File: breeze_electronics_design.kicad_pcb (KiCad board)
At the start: 2 copper layers, 0 parts

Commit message: Delete the footprint of components
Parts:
- added ANT1: Antenna, Footprint:SMD_AN9520, F.Cu at (178.3, 103.0)
- added C1: 0.1UF, Capacitors_SMD:C_0402, F.Cu at (215.7, 133.5)
- added C10: 10UF, Capacitors_SMD:C_1206, F.Cu at (183.8, 111.7)
- added C11: 0.1UF, Capacitors_SMD:C_0402, F.Cu at (234.8, 127.1)
- added C12: 2.2UF, Capacitors_SMD:C_0402, F.Cu at (253.6, 98.1)
- added C13: 220PF, Capacitors_SMD:C_0402, F.Cu at (249.0, 109.3)
- added C14: 2.2UF, Capacitors_SMD:C_0402, F.Cu at (241.8, 115.0)
- added C15: 0.1UF, Capacitors_SMD:C_0402, F.Cu at (217.7, 139.0)
- added C16: 2.2UF, Capacitors_SMD:C_0402, F.Cu at (230.0, 127.1)
- added C17: 220NF, Capacitors_SMD:C_0402, F.Cu at (235.0, 121.6)
- added C18: 0.1UF, Capacitors_SMD:C_0402, F.Cu at (251.4, 103.6)
- added C19: 4.7UF, Capacitors_SMD:C_0402, F.Cu at (230.0, 121.6)
- added C2: 2.2UF, Capacitors_SMD:C_0402, F.Cu at (232.2, 132.6)
- added C20: 2.2UF, Capacitors_SMD:C_0402, F.Cu at (212.9, 139.2)
- added C21: 2.2UF, Capacitors_SMD:C_0402, F.Cu at (237.0, 116.1)
- added C22: 2.2NF, Capacitors_SMD:C_0402, F.Cu at (243.9, 109.5)
- added C23: 2.2UF, Capacitors_SMD:C_0402, F.Cu at (208.1, 145.6)
- added C24: 0.1UF, Capacitors_SMD:C_0402, F.Cu at (221.7, 131.1)
- added C25: 2.2UF, Capacitors_SMD:C_0402, F.Cu at (212.9, 144.7)
- added C26: 22PF, Capacitors_SMD:C_0402, F.Cu at (239.4, 109.5)
- added C27: 2.2NF, Capacitors_SMD:C_0402, F.Cu at (246.5, 103.8)
- added C28: 4.7PF, Capacitors_SMD:C_0402, F.Cu at (202.3, 145.8)
- added C29: 22PF, Capacitors_SMD:C_0402, F.Cu at (232.4, 116.1)
- added C3: 2.2UF, Capacitors_SMD:C_0402, F.Cu at (225.1, 125.6)
- added C30: 1.5PF, Capacitors_SMD:C_0402, F.Cu at (208.1, 140.1)
- added C31: 1PF, Capacitors_SMD:C_0402, F.Cu at (221.0, 125.6)
- added C32: 0.1UF, Capacitors_SMD:C_0402, F.Cu at (248.8, 98.1)
- added C33: 2.2UF, Capacitors_SMD:C_0402, F.Cu at (192.1, 146.6)
- added C4: 2.2UF, Capacitors_SMD:C_0402, F.Cu at (217.7, 144.5)
- added C5: 2.2UF, Capacitors_SMD:C_0402, F.Cu at (227.4, 132.6)
- added C6: 0.1UF, Capacitors_SMD:C_0402, F.Cu at (240.1, 121.6)
- added C7: 2.2UF, Capacitors_SMD:C_0402, F.Cu at (222.5, 136.6)
- added C8: 0.1UF, Capacitors_SMD:C_0402, F.Cu at (246.6, 115.0)
- added C9: 10UF, Capacitors_SMD:C_1206, F.Cu at (215.0, 114.0)
- added D1: MBR0520, Diodes_SMD:SOD-123, F.Cu at (200.3, 124.6)
- added D2: MBR0520, Diodes_SMD:SOD-123, F.Cu at (216.2, 107.5)
- added H1: Header, Pin_Headers:Pin_Header_Straight_1x02, F.Cu at (200.9, 101.5)
- added J1: SIP4, Pin_Headers:Pin_Header_Straight_1x04, F.Cu at (162.0, 125.4)
- added L1: 4.7UH, Footprint:SMD_L0402, F.Cu at (222.4, 141.9)
- added L2: 8.2NH, Footprint:SMD_L0402, F.Cu at (244.8, 120.3)
- added L3: 2.7NH, Footprint:SMD_L0402, F.Cu at (239.5, 126.9)
- added L4: 3.9NH, Footprint:SMD_L0402, F.Cu at (251.3, 114.6)
- added LED1: POWER, LEDs:LED_0603, F.Cu at (166.8, 132.6)
- added LED10: BT_LED, LEDs:LED_0603, F.Cu at (199.3, 137.3)
- added LED11: CHG_LED, LEDs:LED_0603, F.Cu at (186.1, 142.7)
- added LED2: M1_LED_TOP, LEDs:LED_0603, F.Cu at (184.2, 124.1)
- added LED3: M1_LED_BOT, LEDs:LED_0603, F.Cu at (174.5, 129.2)
- added LED4: M2_LED_TOP, LEDs:LED_0603, F.Cu at (179.4, 134.3)
- added LED5: M2_LED_BOT, LEDs:LED_0603, F.Cu at (184.2, 129.2)
- added LED6: M3_LED_TOP, LEDs:LED_0603, F.Cu at (194.9, 119.0)
- added LED7: M3_LED_BOT, LEDs:LED_0603, F.Cu at (207.6, 108.6)
- added LED8: M4_LED_TOP, LEDs:LED_0603, F.Cu at (174.5, 124.1)
- added LED9: M4_LED_BOT, LEDs:LED_0603, F.Cu at (185.2, 119.0)
- added M1: MotorA, Pin_Headers:Pin_Header_Straight_1x02, F.Cu at (177.6, 116.8)
- added M2: MotorA, Pin_Headers:Pin_Header_Straight_1x02, F.Cu at (189.5, 101.5)
- added M3: MotorB, Pin_Headers:Pin_Header_Straight_1x02, F.Cu at (166.8, 125.4)
- added M4: MotorB, Pin_Headers:Pin_Header_Straight_1x02, F.Cu at (195.1, 101.5)
- added Q1: S8050, TO_SOT_Packages_SMD:SOT-23, F.Cu at (206.7, 121.7)
- added Q2: SI2302, TO_SOT_Packages_SMD:SOT-23, F.Cu at (233.1, 98.6)
- added Q3: SI2302, TO_SOT_Packages_SMD:SOT-23, F.Cu at (212.3, 121.7)
- added Q4: SI2302, TO_SOT_Packages_SMD:SOT-23, F.Cu at (193.6, 140.5)
- added Q5: SI2302, TO_SOT_Packages_SMD:SOT-23, F.Cu at (207.0, 128.3)
- added R1: 10K, Resistors_SMD:R_0402, F.Cu at (219.2, 114.3)
- added R10: 100, Resistors_SMD:R_0402, F.Cu at (241.2, 98.2)
- added R11: 100, Resistors_SMD:R_0402, F.Cu at (235.5, 104.8)
- added R12: 100, Resistors_SMD:R_0402, F.Cu at (205.3, 134.5)
- added R13: 10K, Resistors_SMD:R_0402, F.Cu at (228.6, 105.2)
- added R14: 3K, Resistors_SMD:R_0402, F.Cu at (225.2, 120.0)
- added R15: 100, Resistors_SMD:R_0402, F.Cu at (237.7, 98.2)
- added R16: 3K, Resistors_SMD:R_0402, F.Cu at (222.7, 114.3)
- added R17: 100, Resistors_SMD:R_0402, F.Cu at (232.0, 104.8)
- added R18: 3K, Resistors_SMD:R_0402, F.Cu at (242.4, 103.9)
- added R19: 22K, Resistors_SMD:R_0402, F.Cu at (216.9, 120.2)
- added R2: 33K, Resistors_SMD:R_0402, F.Cu at (217.5, 125.9)
- added R20: 33K, Resistors_SMD:R_0402, F.Cu at (235.5, 110.5)
- added R21: 33K, Resistors_SMD:R_0402, F.Cu at (238.9, 103.9)
- added R22: 33K, Resistors_SMD:R_0402, F.Cu at (244.6, 98.2)
- added R23: 33K, Resistors_SMD:R_0402, F.Cu at (211.6, 133.6)
- added R3: 33K, Resistors_SMD:R_0402, F.Cu at (203.9, 140.2)
- added R4: 33K, Resistors_SMD:R_0402, F.Cu at (232.0, 110.5)
- added R5: 10K, Resistors_SMD:R_0402, F.Cu at (214.1, 127.9)
- added R6: 1.65K, Resistors_SMD:R_0402, F.Cu at (221.1, 120.0)
- added R7: 10K, Resistors_SMD:R_0402, F.Cu at (198.2, 142.7)
- added R8: 3K, Resistors_SMD:R_0402, F.Cu at (211.1, 127.9)
- added R9: 100, Resistors_SMD:R_0402, F.Cu at (228.6, 110.9)
- added S1: SW2X3, Footprint:DIP_SW2x3, F.Cu at (184.0, 101.7)
- added U1: MIC5205-3.3, TO_SOT_Packages_SMD:SOT-23-5, F.Cu at (209.1, 98.9)
- added U10: NRF24L01, Footprint:QFN_NRF24L01, F.Cu at (178.8, 141.2)
- added U11: HM_Bluetooth, Footprint:SMD_HM, F.Cu at (167.2, 108.6)
- added U2: STM32F103T8U6TR, Footprint:VFQFPN_STM32F103T8U6TR, F.Cu at (167.3, 140.5)
- added U3: LM27313, TO_SOT_Packages_SMD:SOT-23-5, F.Cu at (226.6, 98.9)
- added U4: LTC4054, TO_SOT_Packages_SMD:SOT-23-5, F.Cu at (223.4, 108.0)
- added U5: CP2102, Footprint:QFN_CP2102, F.Cu at (199.6, 110.9)
- added U6: MIC5205, TO_SOT_Packages_SMD:SOT-23-5, F.Cu at (200.1, 131.3)
- added U7: HMC5883L, Footprint:LPCC_HMC5883L, F.Cu at (206.7, 114.8)
- added U8: MPU6050, Footprint:QFN_MPU6050, F.Cu at (192.8, 125.9)
- added U9: MS5611, Footprint:QFN_MS5611, F.Cu at (187.4, 135.8)
- added USB1: MicroUSB, Connect:USB_Micro-B, F.Cu at (191.6, 110.6)
- added X1: 16MHZ, Footprint:SMD_XTAL3225, F.Cu at (193.3, 133.8)
- added Y1: 8MHZ, Crystals:Resonator_7.2x3mm, F.Cu at (218.6, 99.9)

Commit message: Add the shape of breeze in PCB
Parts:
- M2: value MotorA -> MotorB
- M3: value MotorB -> MotorA
- moved C33 82.5 mm to (261.7, 102.2)
- moved LED1 61.5 mm to (228.2, 135.9)
- moved C30 59.5 mm to (258.1, 107.9)
- moved C32 56.5 mm to (217.9, 145.4)
- moved R10 55.6 mm to (210.3, 144.5)
- moved C4 52.1 mm to (263.0, 118.7)
- moved C3 47.5 mm to (266.5, 102.2)
- moved LED11 47.0 mm to (226.0, 117.9)
- moved R3 46.3 mm to (243.4, 116.0)
- moved C15 44.7 mm to (257.6, 118.9)
- moved Q1 43.8 mm to (246.2, 102.8)
- moved C12 43.0 mm to (233.5, 136.1)
- moved R7 39.8 mm to (233.7, 124.8)
- moved Q5 38.8 mm to (241.1, 109.8)
- moved Q4 36.2 mm to (225.7, 123.7)
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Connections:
- Q3 pad 3: Net-(M2-Pad2) -> Net-(M3-Pad2)
- Q4 pad 3: Net-(M3-Pad1) -> Net-(M2-Pad1)
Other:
- board outline added: 104.1 x 104.1 mm

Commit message: Add the motor's base
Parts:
- added ?: , Footprint:PTH_Motor, F.Cu at (5.08, 5.08)
- added ?: , Footprint:PTH_Motor, F.Cu at (5.08, 94.9)
- added ?: , Footprint:PTH_Motor, F.Cu at (94.9, 94.9)
- added ?: , Footprint:PTH_Motor, F.Cu at (94.9, 5.08)
- moved C15 82.8 mm to (263.8, 36.3)
- moved C29 82.8 mm to (241.5, 47.8)
- moved C6 82.8 mm to (263.4, 41.8)
- moved J1 82.8 mm to (181.4, 46.9)
- moved L2 82.8 mm to (260.4, 47.5)
- moved L3 82.8 mm to (255.5, 53.0)
- moved L4 82.8 mm to (249.2, 58.5)
- moved LED1 82.8 mm to (234.4, 53.3)
- moved M3 82.8 mm to (186.2, 46.9)
- moved R22 82.8 mm to (245.7, 39.1)
- moved R23 82.8 mm to (229.9, 53.0)
- moved U10 82.8 mm to (198.2, 62.7)
- moved U6 82.8 mm to (205.5, 64.0)
- moved U7 82.8 mm to (207.5, 56.8)
- moved ANT1 82.8 mm to (197.7, 24.5)
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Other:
- board text added: "M1"
- board text added: "M2"
- board text added: "M3"

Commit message: Finish the layout of LEDs and Motors
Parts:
- moved M1 344.6 mm to (-81.2, -79.7)
- moved R9 340.1 mm to (-68.0, -75.4), turned to 45 degrees
- moved R20 333.5 mm to (-75.1, -68.2), turned to 45 degrees
- moved Q2 328.2 mm to (-71.6, -71.6), turned to 45 degrees
- moved R22 320.1 mm to (-68.0, -24.9), turned to 135 degrees
- moved Q4 311.3 mm to (-71.6, -28.4), turned to 135 degrees
- moved R10 306.6 mm to (-75.4, -32.0), turned to 135 degrees
- moved LED2 306.3 mm to (-77.1, -77.1), turned to 45 degrees
- moved LED3 296.2 mm to (-74.6, -74.6), turned to 45 degrees
- moved R11 295.3 mm to (-31.8, -24.4), turned to 225 degrees
- moved Q5 292.6 mm to (-28.1, -71.8), turned to 315 degrees
- moved M2 291.4 mm to (-79.4, -18.8), turned to 225 degrees
- moved R23 291.2 mm to (-31.5, -75.4), turned to 315 degrees
- moved R21 290.2 mm to (-24.4, -31.5), turned to 225 degrees
- moved LED4 290.1 mm to (-77.1, -22.9), turned to 135 degrees
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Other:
- board text added: "M4"

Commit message: Finish the layout of Wireless
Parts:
- U11: footprint Footprint:SMD_HM -> SMD_HM
- moved C18 434.7 mm to (-173.7, -39.1)
- moved C17 429.6 mm to (-173.7, -58.4)
- moved C19 427.6 mm to (-159.0, -55.4)
- moved C21 427.2 mm to (-153.9, -34.5)
- moved C22 424.6 mm to (-154.4, -39.1)
- moved R8 422.2 mm to (-173.7, -34.0)
- moved C16 421.5 mm to (-173.7, -43.7)
- moved R18 413.6 mm to (-151.4, -43.7)
- moved C20 413.3 mm to (-158.5, -34.5)
- moved C24 401.8 mm to (-150.9, -55.4)
- moved C23 399.5 mm to (-150.9, -59.9)
- moved R14 396.4 mm to (-159.0, -59.4)
- moved R16 395.3 mm to (-157.5, -43.7)
- moved U7 390.4 mm to (-165.1, -59.4)
- moved U8 387.7 mm to (-165.1, -42.2)
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
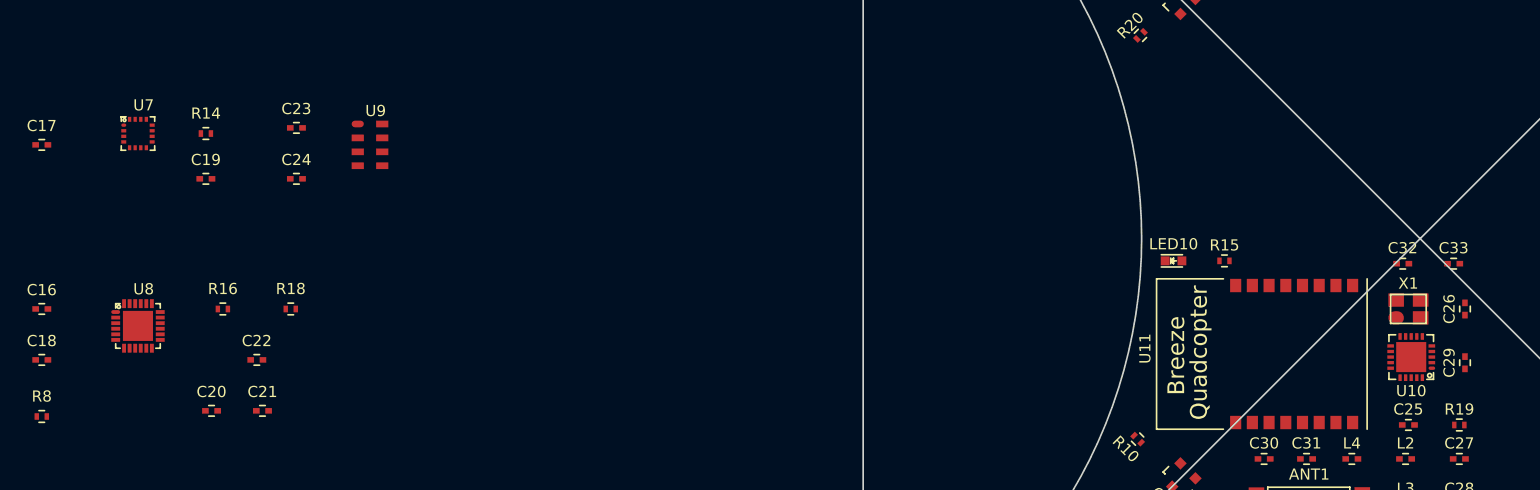
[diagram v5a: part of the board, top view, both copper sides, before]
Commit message: Finish the layout of Sensors
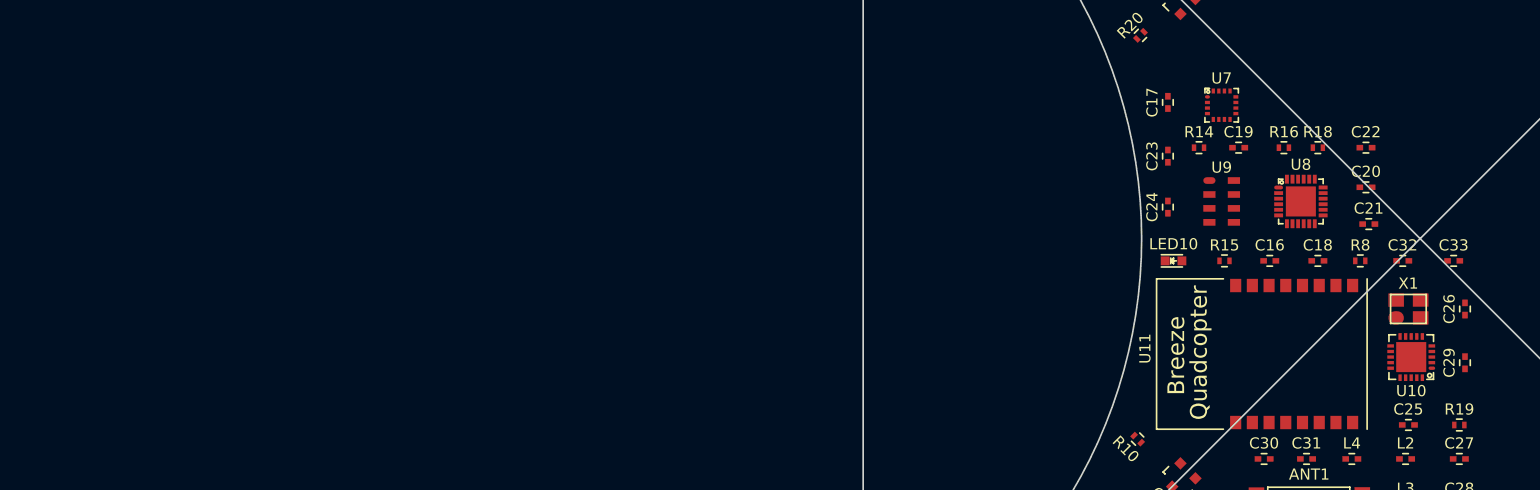
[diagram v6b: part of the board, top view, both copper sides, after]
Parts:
- moved R8 119.2 mm to (-55.4, -48.0)
- moved C18 114.9 mm to (-59.2, -48.0)
- moved C16 110.3 mm to (-63.5, -48.0)
- moved C20 105.6 mm to (-54.9, -54.6)
- moved U8 105.0 mm to (-60.7, -53.3)
- moved C22 101.4 mm to (-54.9, -58.2)
- moved C17 101.2 mm to (-72.6, -62.2), turned to 90 degrees
- moved C21 100.7 mm to (-54.6, -51.3)
- moved U7 97.3 mm to (-67.8, -62.0)
- moved R16 96.3 mm to (-62.2, -58.2)
- moved R18 93.3 mm to (-59.2, -58.2)
- moved C19 92.8 mm to (-66.3, -58.2)
- moved R14 89.2 mm to (-69.8, -58.2)
- moved C23 78.3 mm to (-72.6, -57.4), turned to 90 degrees
- moved C24 78.3 mm to (-72.6, -52.8), turned to 90 degrees
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
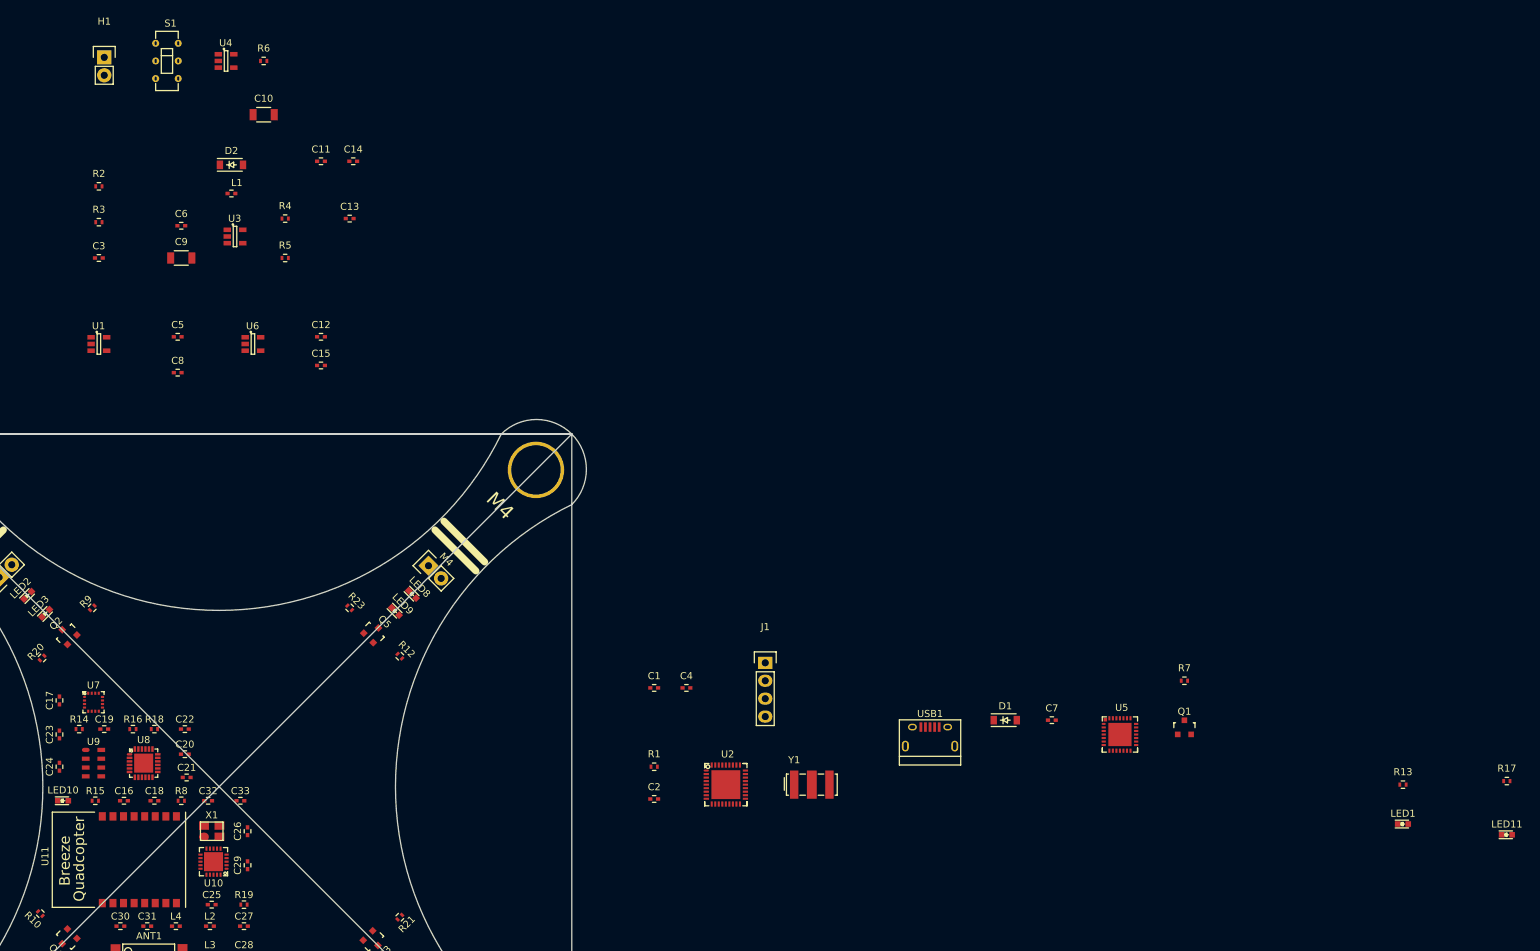
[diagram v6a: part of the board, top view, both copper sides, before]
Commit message: Finish the layout of Power
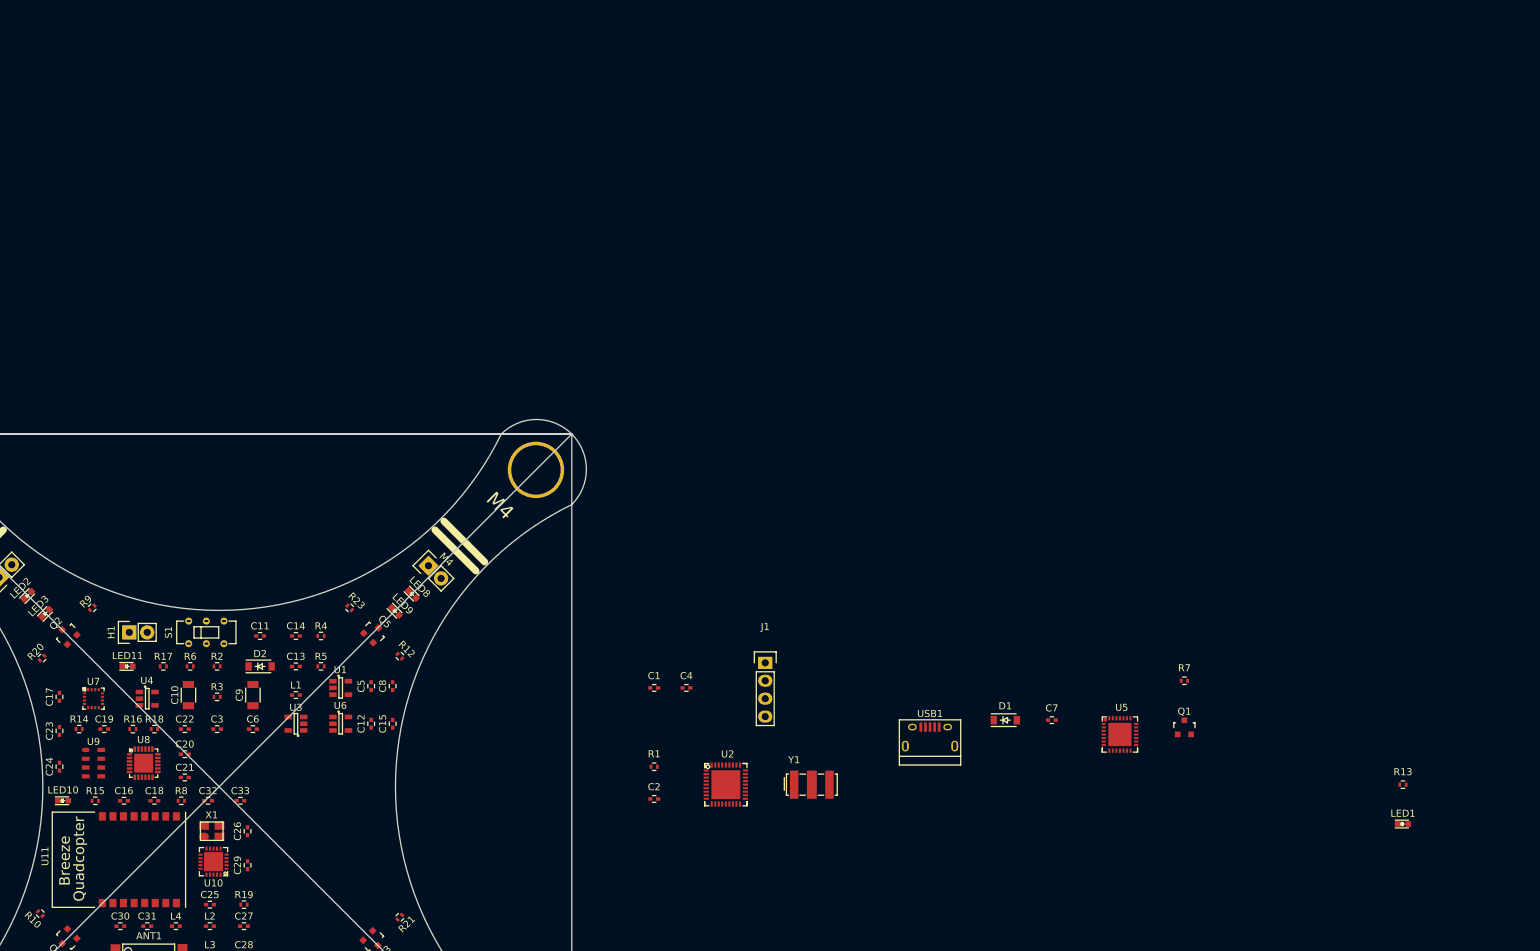
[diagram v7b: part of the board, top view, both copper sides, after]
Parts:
- moved LED11 197.0 mm to (-63.0, -67.1)
- moved R17 191.2 mm to (-57.9, -67.1)
- moved U4 91.1 mm to (-60.2, -62.5)
- moved R6 86.5 mm to (-54.1, -67.1)
- moved C10 83.0 mm to (-54.4, -63.0), turned to 90 degrees
- moved H1 81.6 mm to (-62.7, -71.9), turned to 90 degrees
- moved S1 81.2 mm to (-51.8, -71.9), turned to 90 degrees
- moved C6 72.1 mm to (-45.2, -58.2)
- moved L1 71.7 mm to (-39.1, -63.0)
- moved D2 71.2 mm to (-44.2, -67.1)
- moved R2 70.1 mm to (-50.3, -67.1)
- moved U3 69.6 mm to (-39.1, -58.9), turned to 180 degrees
- moved R3 69.4 mm to (-50.3, -62.7)
- moved C3 68.9 mm to (-50.3, -58.2)
- moved C11 67.9 mm to (-44.2, -71.4)
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
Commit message: Finish the layout of PCB
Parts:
- moved R13 151.6 mm to (-32.3, -71.4)
- moved LED1 148.0 mm to (-28.4, -67.3)
- moved Q1 125.7 mm to (-37.8, -42.4)
- moved R7 122.1 mm to (-33.3, -43.4)
- moved U5 120.8 mm to (-41.4, -37.3)
- moved C7 111.6 mm to (-42.4, -43.4)
- moved D1 99.6 mm to (-35.6, -37.1), turned to 90 degrees
- moved USB1 82.1 mm to (-29.0, -37.3), turned to 90 degrees
- moved Y1 76.5 mm to (-42.4, -52.8), turned to 90 degrees
- moved J1 56.4 mm to (-27.2, -53.6)
- moved U2 54.6 mm to (-32.8, -49.0)
- moved C2 49.8 mm to (-38.1, -46.2)
- moved R1 49.8 mm to (-38.1, -51.3)
- moved C4 48.2 mm to (-31.0, -54.6)
- moved C1 47.7 mm to (-35.1, -54.6)
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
